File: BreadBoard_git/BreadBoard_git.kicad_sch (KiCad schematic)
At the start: 36 parts, among them Q1 CSD18512Q5B, Q2 CSD18512Q5B, Q3 RQ3E110AJTB, Q4 RQ3E110AJTB, Q5 RQ3E110AJTB, U1 ESP32-S3, U2 LM73605RNPR, U3 LM5148RGYR

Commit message: update
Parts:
- added J1: SHT45 breakout, symbol Connector:Conn_01x05_Pin
- added J2: Conn_01x15_Pin, symbol Connector:Conn_01x15_Pin
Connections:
- new net 3Vo: J2.3 (Pin_3)
- new net 3vo: J1.2 (Pin_2)
- new net CD: J2.8 (Pin_8)
- new net INT: J2.11 (Pin_11)
- new net LITE: J2.4 (Pin_4)
- new net MISO: J2.6 (Pin_6)
- new net MOSI: J2.7 (Pin_7)
- new net RST: J2.9 (Pin_9)
- new net SCK: J2.5 (Pin_5)
- new net SCL: J1.4 (Pin_4)
- new net SDA: J1.5 (Pin_5)
- new net VIN: J1.1 (VIN), J2.1 (Pin_1)
- new net WAIT: J2.10 (Pin_10)
- new net X+: J2.15 (Pin_15)
- new net X-: J2.14 (Pin_14)
- new net Y+: J2.12 (Pin_12)
- new net Y-: J2.13 (Pin_13)
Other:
- moved on the sheet: Q3, Q4, Q5, U1

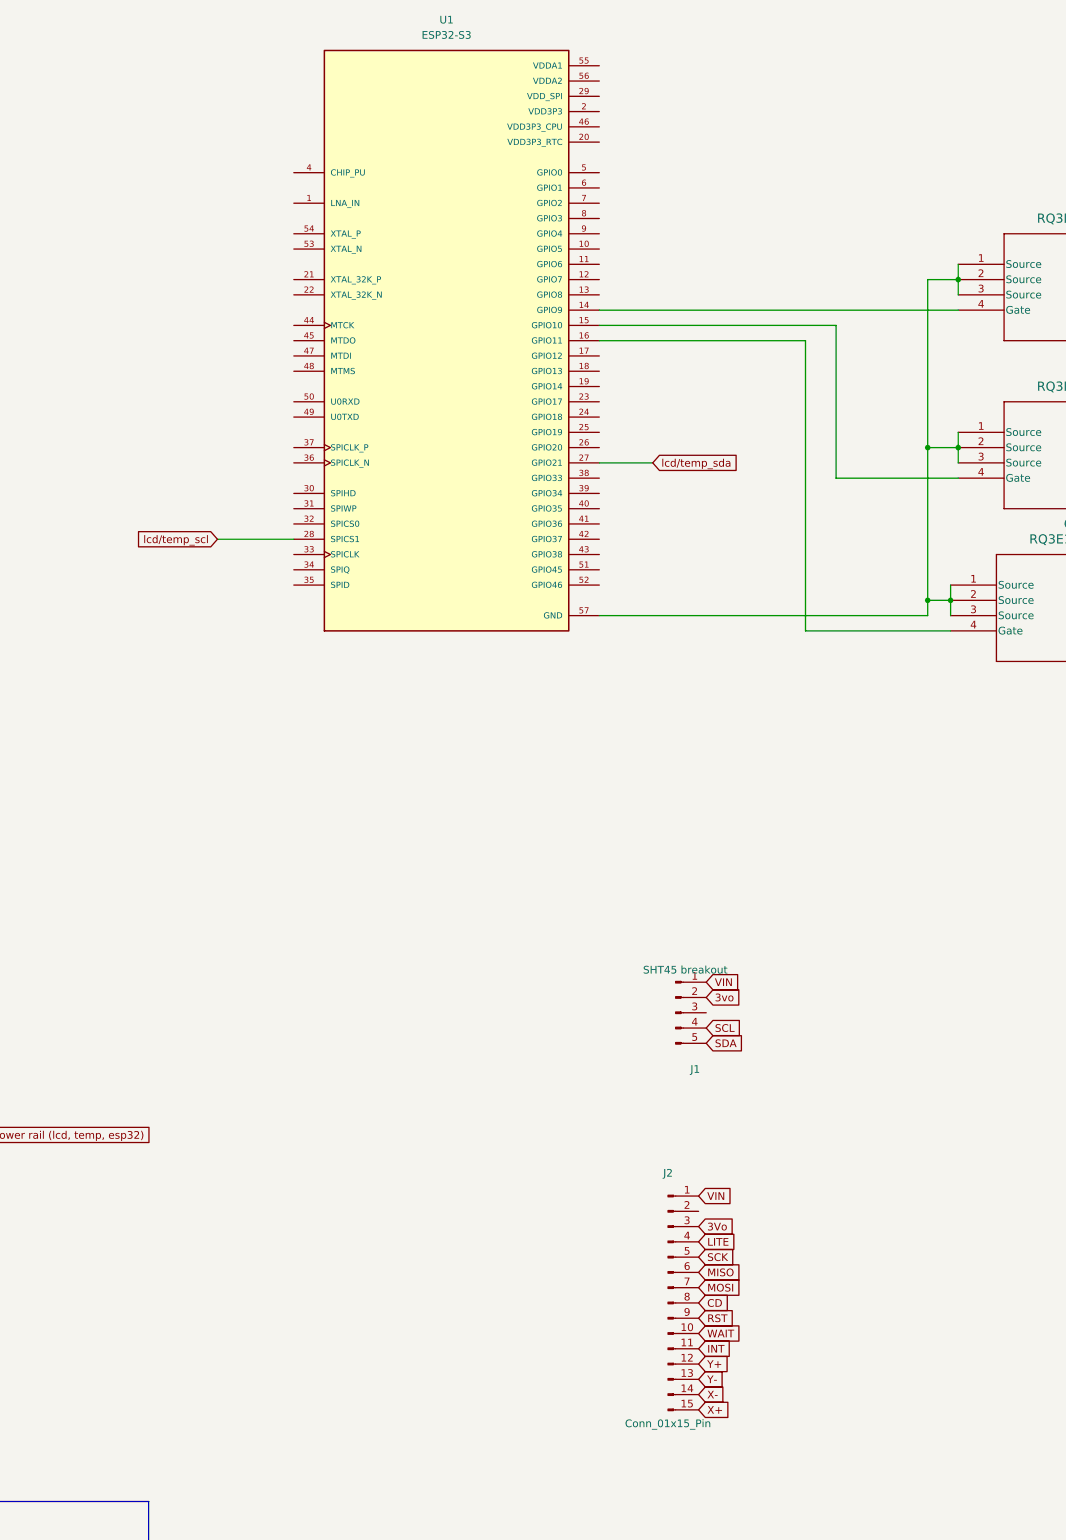
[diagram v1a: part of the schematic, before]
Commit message: lcd driver
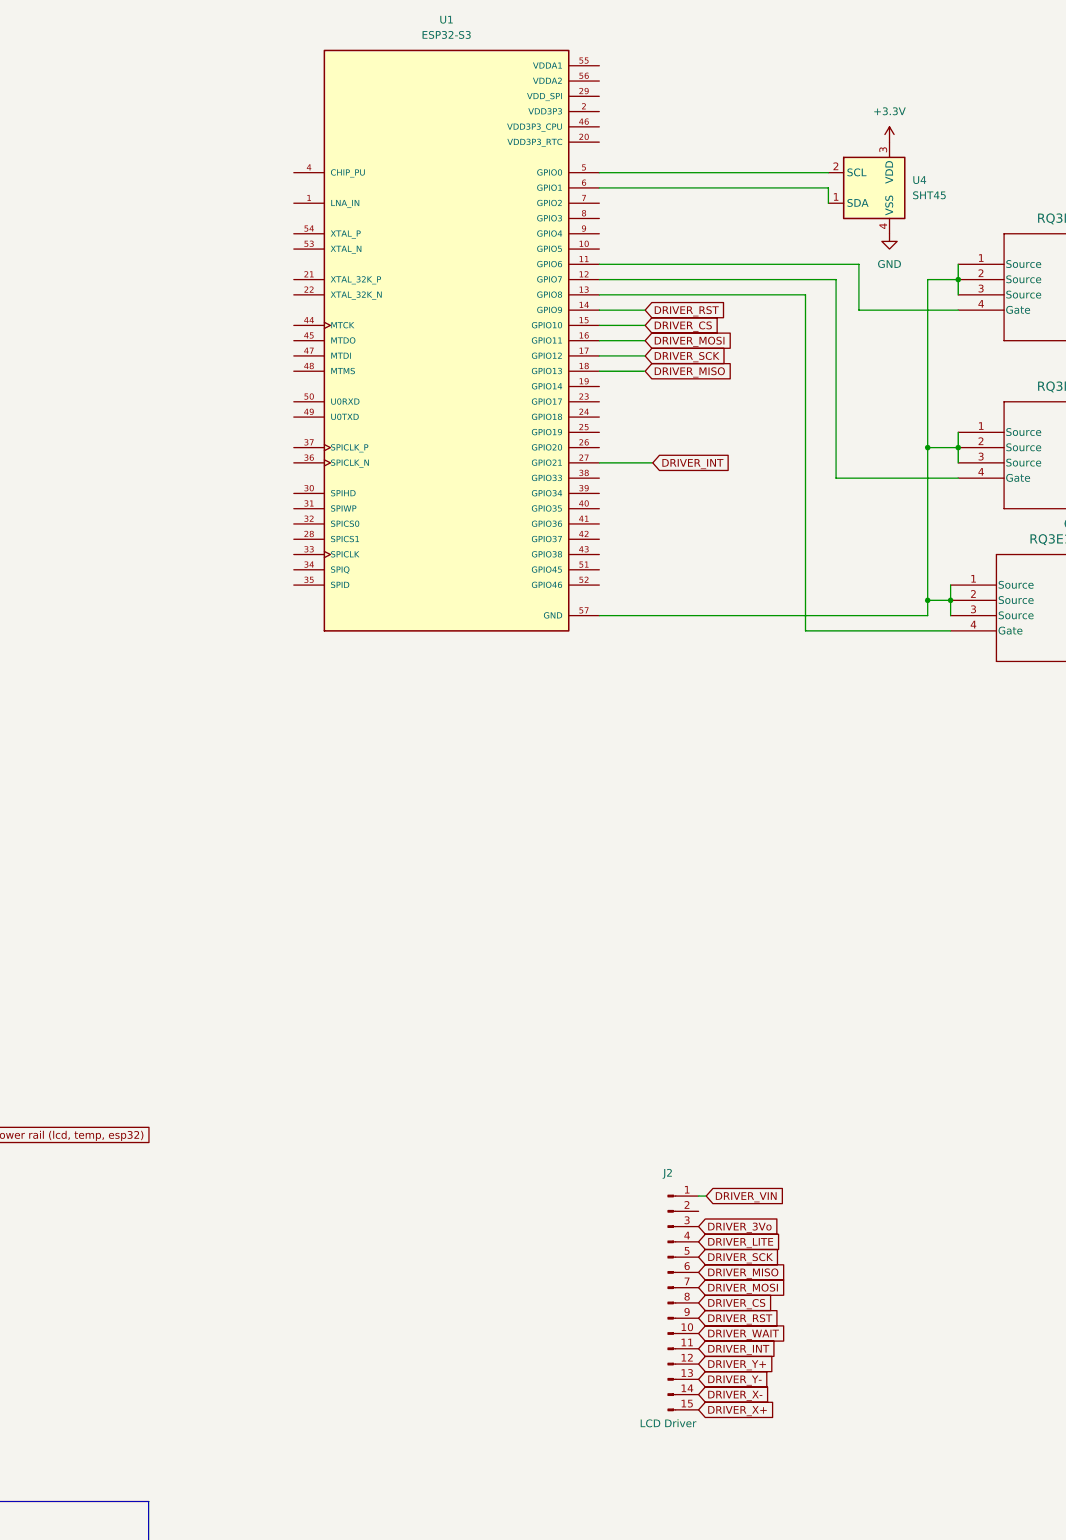
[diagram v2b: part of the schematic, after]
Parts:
- removed J1: SHT45 breakout, symbol Connector:Conn_01x05_Pin
- added U4: SHT45, Sensor_Humidity:Sensirion_DFN-4_1.5x1.5mm_P0.8mm_SHT4x_NoCentralPad, symbol Sensor_Humidity:SHT4x
- J2: value Conn_01x15_Pin -> LCD Driver
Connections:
- net MISO is gone; now on net DRIVER_MISO: J2.6 (Pin_6)
- net RST is gone; now on net DRIVER_RST: J2.9 (Pin_9)
- net SCK is gone; now on net DRIVER_SCK: J2.5 (Pin_5)
- net lcd/temp_sda is gone; now on net DRIVER_INT: U1.27 (GPIO21)
- net DAP: now also U4.4 (VSS)
- net at Q4.4 (Gate): now also U1.12 (GPIO7); no longer U1.15 (GPIO10)
- net at Q5.4 (Gate): now also U1.13 (GPIO8); no longer U1.16 (GPIO11)
- net at U1.11 (GPIO6): now also Q3.4 (Gate)
- net DRIVER_RST: now reaches U1.14 (GPIO9)
- net DRIVER_RST: no longer Q3.4 (Gate)
- net DRIVER_SCK: now reaches U1.17 (GPIO12)
- net DRIVER_MISO: now reaches U1.18 (GPIO13)
- net at U1.5 (GPIO0): now also U4.2 (SCL)
- net at U1.6 (GPIO1): now also U4.1 (SDA)
- net 3Vo renamed DRIVER_3Vo
- net CD renamed DRIVER_CS
- net DRIVER_CS: now also U1.15 (GPIO10)
- net INT renamed DRIVER_INT
- net LITE renamed DRIVER_LITE
- net MOSI renamed DRIVER_MOSI
- net DRIVER_MOSI: now also U1.16 (GPIO11)
- net VIN renamed DRIVER_VIN
- net WAIT renamed DRIVER_WAIT
- net X+ renamed DRIVER_X+
- net X- renamed DRIVER_X-
- net Y+ renamed DRIVER_Y+
- net Y- renamed DRIVER_Y-
- net lcd/temp_scl: no longer names the net of U1.28 (SPICS1)
- new net +3.3V: U4.3 (VDD)

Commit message: updated schmatic
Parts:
- removed Iout: 1, symbol Simulation_SPICE:IDC
- removed L1: L, symbol Device:L
- added D2: SMBJ28A, SMBJ28A:DIOM5436X244N, symbol SMBJ28A:SMBJ28A
- added F1: 0.1 Omh, symbol Device:Fuse
- added J1: 24V DC wall plug-iN, symbol Connector_Generic:Conn_01x02
- added L2: 3.9uH, symbol Device:L
- Cboot, Cvdda: value C -> 100nF
- Cboot1: renamed from Cboot; value C -> 470nF
- Cbulk1: renamed from Cbulk; value C_US -> 100uF
- Ccomp: value C -> 820.0pF
- Ccomp2: renamed from Ccomp; value C -> 30.0pF
- Cff1: renamed from Cff; value C -> 16pF
- Cin: value C -> 1.5uF
- Cin2: renamed from Cin; value C -> 10uF (2)
- Cinx2: renamed from Cinx; value C -> 47nF
- Cout: value C -> 10uF
- Cout1: renamed from Cout; value C_US -> 100uF
- Coutx2: renamed from Coutx; value C -> 470nF
- Cvcc: value C -> 2.2uF
- Cvcc1: renamed from Cvcc; value C -> 2.2uF
- L1: value L -> 680nH
- Rcomp: renamed from Rconfig1; value R -> 4.87kOhm
- Rconfig: value R -> 40.2kOhm
- Rfbb1: renamed from Rfbb; value R -> 43.2kOhm
- Rfbt1: renamed from Rfbt; value R -> 100kOhm
- Rpg: value R -> 100kOmh
- Rpgood1: renamed from Rpgood; value R -> 105kOhm
- Rsense: value R -> 3.0Ohm
- Rt: value R -> 9.53kOhm
- Rvdda: value R -> 47.5kOmh
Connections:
- net DAP: now also J1.2 (GND); no longer Cff1.1, Cout1.1, Coutx2.1, Rfbt1.2, Rpgood1.2
- net Heater Vcc: now reaches Cout.1, Rsense.2, U3.21 (VOUT)
- net at Cboot1.2, U2.1 (SW_1), U2.2 (SW_2)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: now also L2.1
- new net: D2.A, F1.2
- new net: F1.1, J1.1 (24+)
- new net 3.3V: Cff1.1, Cout1.1, Coutx2.1, L2.2, Rfbt1.2, Rpgood1.2
- no-connect marks 1 -> 46
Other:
- note added: "3.3V Buck"
- note added: "Power Input"
- moved on the sheet: Cboot1, Cbulk1, Cff1, Cin2, Cinx2, Cout1, Coutx2, Cvcc1, Rfbb1, Rfbt1, Rpgood1, U2

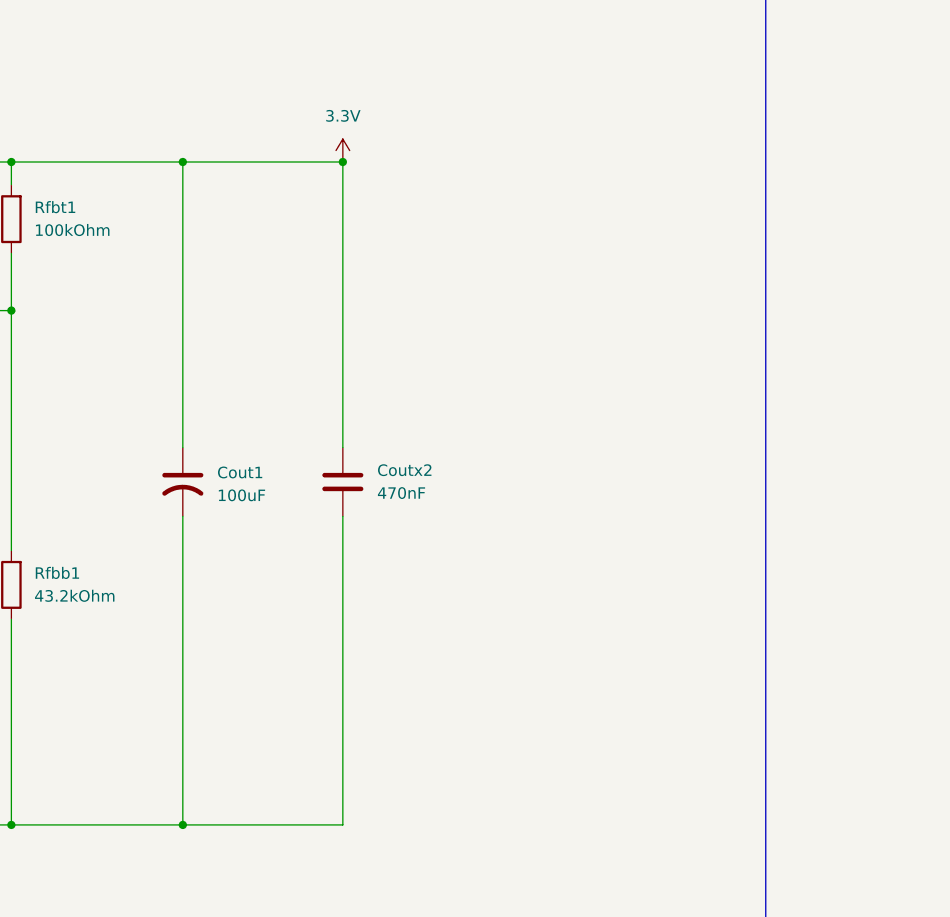
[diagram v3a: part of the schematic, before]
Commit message: add footprint cout
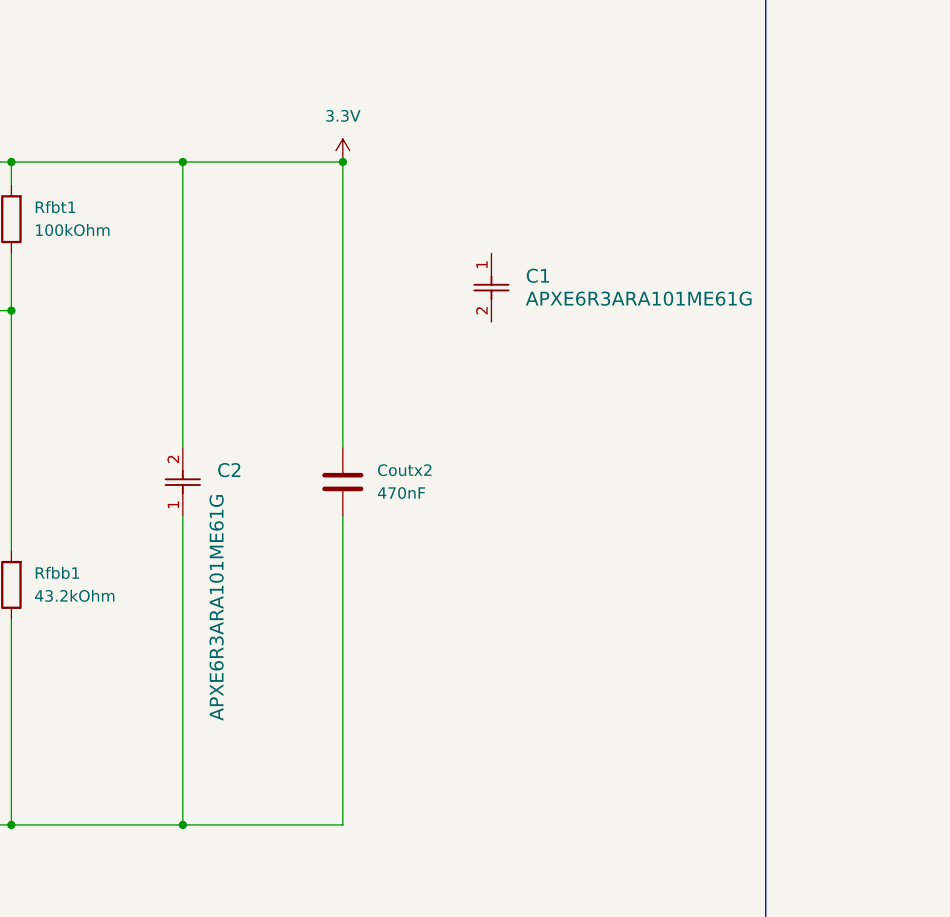
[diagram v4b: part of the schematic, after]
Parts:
- removed Cout1: 100uF, symbol Device:C_US
- added C1, C2: APXE6R3ARA101ME61G, CHEMI-E61, symbol cout:APXE6R3ARA101ME61G
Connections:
- net 3.3V: now also C2.2
- net DAP: now also C2.1
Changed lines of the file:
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@@
 	)
 	(junction
+		(at 256.54 110.49)
+		(diameter 0)
+		(color 0 0 0 0)
+	)
+	(junction
 		(at 203.2 110.49)
 		(diameter 0)
@@
 	)
 	(junction
-		(at 256.54 110.49)
-		(diameter 0)
-		(color 0 0 0 0)
-	)
-	(junction
 		(at 525.78 90.17)
 		(diameter 0)
@@
 	(wire
 		(pts
+			(xy 256.54 110.49) (xy 274.32 110.49)
+		)
+		(stroke
+			(width 0)
+			(type default)
+		)
+	)
+	(wire
+		(pts
 			(xy 100.33 342.9) (xy 100.33 354.33)
 		)
@@
 	(wire
 		(pts
+			(xy 256.54 110.49) (xy 256.54 142.24)
+		)
+		(stroke
+			(width 0)
+			(type default)
+		)
+	)
+	(wire
+		(pts
 			(xy 425.45 49.53) (xy 463.55 49.53)
 		)
@@
 	(wire
 		(pts
-			(xy 256.54 110.49) (xy 274.32 110.49)
-		)
-		(stroke
-			(width 0)
-			(type default)
-		)
-	)
-	(wire
-		(pts
 			(xy 464.82 64.77) (xy 464.82 97.79)
 		)
@@
 	(wire
 		(pts
-			(xy 256.54 142.24) (xy 256.54 110.49)
-		)
-		(stroke
-			(width 0)
-			(type default)
-		)
-	)
-	(wire
-		(pts
 			(xy 370.84 300.99) (xy 370.84 307.34)
 		)
@@
 	)
 	(symbol
-		(lib_id "Device:C_US")
-		(at 256.54 146.05 0)
-		(unit 1)
-		(exclude_from_sim no)
-		(in_bom yes)
-		(on_board yes)
-		(dnp no)
-		(fields_autoplaced yes)
-		(property "Reference" "Cout1"
-			(at 260.35 145.0339 0)
-			(effects
-				(font
-					(size 1.27 1.27)
-				)
-				(justify left)
-			)
-		)
-		(property "Value" "100uF"
-			(at 260.35 147.5739 0)
-			(effects
-				(font
-					(size 1.27 1.27)
-				)
-				(justify left)
-			)
-		)
-		(property "Footprint" ""
-			(at 256.54 146.05 0)
-			(effects
-				(font
-					(size 1.27 1.27)
-				)
-				(hide yes)
-			)
-		)
-		(property "Datasheet" ""
-			(at 256.54 146.05 0)
-			(effects
-				(font
-					(size 1.27 1.27)
-				)
-				(hide yes)
-			)
-		)
-		(property "Description" "capacitor, US symbol"
-			(at 256.54 146.05 0)
-			(effects
-				(font
-					(size 1.27 1.27)
-				)
-				(hide yes)
-			)
-		)
-		(pin "1"
-		)
-		(pin "2"
-		)
-		(instances
-			(project "BreadBoard_git"
-				(path "/f1e91c7e-2505-4703-8fd4-3771cb631fb1"
-					(reference "Cout1")
-					(unit 1)
-				)
-			)
-		)
-	)
-	(symbol
 		(lib_id "Device:C")
 		(at 308.61 337.82 0)
@@
 	)
 	(symbol
+		(lib_id "cout:APXE6R3ARA101ME61G")
+		(at 290.83 120.65 270)
+		(unit 1)
+		(exclude_from_sim no)
+		(in_bom yes)
+		(on_board yes)
+		(dnp no)
+		(property "Reference" "C1"
+			(at 294.64 123.1899 90)
+			(effects
+				(font
+					(size 1.524 1.524)
+				)
+				(justify left)
+			)
+		)
+		(property "Value" "APXE6R3ARA101ME61G"
+			(at 294.64 125.7299 90)
+			(effects
+				(font
+					(size 1.524 1.524)
+				)
+				(justify left)
+			)
+		)
+		(property "Footprint" "CHEMI-E61"
+			(at 290.83 120.65 0)
+			(effects
+				(font
+					(size 1.27 1.27)
+					(italic yes)
+				)
+				(hide yes)
+			)
+		)
+		(property "Datasheet" "APXE6R3ARA101ME61G"
+			(at 290.83 120.65 0)
+			(effects
+				(font
+					(size 1.27 1.27)
+					(italic yes)
+				)
+				(hide yes)
+			)
+		)
+		(property "Description" ""
+			(at 290.83 120.65 0)
+			(effects
+				(font
+					(size 1.27 1.27)
+				)
+				(hide yes)
+			)
+		)
+		(pin "2"
+		)
+		(pin "1"
+		)
+		(instances
+			(project ""
+				(path "/f1e91c7e-2505-4703-8fd4-3771cb631fb1"
+					(reference "C1")
+					(unit 1)
+				)
+			)
+		)
+	)
+	(symbol
 		(lib_id "power:GND")
 		(at 49.53 316.23 0)
@@
 					(unit 1)
 				)
+			)
+		)
+	)
+	(symbol
+		(lib_id "cout:APXE6R3ARA101ME61G")
+		(at 256.54 149.86 90)
+		(unit 1)
+		(exclude_from_sim no)
+		(in_bom yes)
+		(on_board yes)
+		(dnp no)
+		(property "Reference" "C2"
+			(at 260.35 144.7799 90)
+			(effects
+				(font
+					(size 1.524 1.524)
+				)
+				(justify right)
+			)
+		)
+		(property "Value" "APXE6R3ARA101ME61G"
+			(at 260.35 147.3199 0)
+			(effects
+				(font
+					(size 1.524 1.524)
+				)
+				(justify right)
+			)
+		)
+		(property "Footprint" "CHEMI-E61"
+			(at 256.54 149.86 0)
+			(effects
+				(font
+					(size 1.27 1.27)
+					(italic yes)
+				)
+				(hide yes)
+			)
+		)
+		(property "Datasheet" "APXE6R3ARA101ME61G"
+			(at 256.54 149.86 0)
+			(effects
+				(font
+					(size 1.27 1.27)
+					(italic yes)
+				)
+				(hide yes)
+			)
+		)
+		(property "Description" ""
+			(at 256.54 149.86 0)
+			(effects
+				(font
+					(size 1.27 1.27)
+				)
+				(hide yes)
+			)
+		)
+		(pin "1"
+		)
+		(pin "2"
+		)
+		(instances
+			(project ""
+				(path "/f1e91c7e-2505-4703-8fd4-3771cb631fb1"
+					(reference "C2")
+					(unit 1)
+				)

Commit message: updte
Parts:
- removed Cboot, Cvdda: 100nF, symbol Device:C
- removed Ccomp: 820.0pF, symbol Device:C
- removed Ccomp2: 30.0pF, symbol Device:C
- removed Cin: 1.5uF, symbol Device:C
- removed Cout: 10uF, symbol Device:C
- removed Cvcc: 2.2uF, symbol Device:C
- removed L1: 680nH, symbol Device:L
- added C3, C9: GRM155R71A104KA01D, GRM155R71A104KA01D:CAPC1005X55N, symbol cboot:GRM155R71A104KA01D
- added C4: CL05C821JB5NNNC, CL05C821JB5NNNC:CAPC1005X55N, symbol ccomp:CL05C821JB5NNNC
- added C5: C0402C300J5GACTU, CAPC10555_55N_KEM, symbol ccomp2:C0402C300J5GACTU
- added C6: C2012X6S1H155K125AB, C2012X6S1H155K125AB:CAPC2012X145N, symbol cin:C2012X6S1H155K125AB
- added C7: MSAST21GBB5106MTNA01, MSAST21GBB5106MTNA01:CAPC2012X145N, symbol cout2:MSAST21GBB5106MTNA01
- added C8: GRM188R71A225KE15D, G-188_MUR, symbol cvcc:GRM188R71A225KE15D
- added L3: CDEP63MENP-R68MC, IND_CDEP63MENP-R68MC_SUM, symbol l1:CDEP63MENP-R68MC
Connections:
- net DAP: now also C6.1, C8.1, C9.1
- net GNDREF: now also C7.1
- net Heater Vcc: now also C7.2
- net at Rcomp.1: now also C4.2
- net at Rcomp.2, U3.5 (EXTCOMP): now also C5.2
- net at Q1.1, Q1.2, Q1.3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: now also C3.1, L3.2
- net at Rsense.1, U3.20 (ISNS+): now also L3.1
- net at Rpg.1, U3.9 (VCC): now also C8.2
- net at Q1.5_8, U3.12 (VIN), U3.19 (EN)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: now also C6.2
- net at Rvdda.2, U3.18 (PFM/SYNC), U3.8 (VDDA): now also C9.2
- net at U3.15 (CBOOT): now also C3.2
- new net: C4.1, C5.1
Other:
- moved on the sheet: Rsense
